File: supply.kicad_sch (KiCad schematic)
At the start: 186 parts, among them J7 BarrelJack_Pin2mm_MJ-179PH, J8 JST_SH_1x4_BM04B-SRSS-TB-LF-SN, Q12 SI7613DN-T1-GE3, Q13 SI7613DN-T1-GE3, Q14 BSS138PW, Q15 BSS138PW, Q16 BSS138PW, Q17 BSS138PW, SW4 SW_CVS-08TB, SW5 SW_KMR211NGLFS_SMD, U17 LTC4412IS6, U18 LTC4412IS6, U19 MPM54304GMN, U20 MPM54304GMN, U21 NCP718BSN330T1G, U22 MAX16150A_SOT, U25 PAC1954T-E_VQFN, U26 MAX812REUS+T, U28 XC6230H001ER-G, U29 MCP4726A0T_DFN, U30 PAC1954T-E_VQFN, U31 LM3880, U36 MP8796B, U37 MP8796B

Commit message: [#66300] Finish reconnecting power supply to support US+ voltages and power sequence
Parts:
- removed C205, C216, C220: C_100n_0402, antmicro-footprints:C_0402_1005Metric, symbol antmicroCapacitors0402:C_100n_0402
- removed C206: C_1u_0402, antmicro-footprints:C_0402_1005Metric, symbol antmicroCapacitors0402:C_1u_0402
- removed C207, C211, C218: C_10u_6.3V_0402, antmicro-footprints:C_0402_1005Metric, symbol antmicroCapacitors0402:C_10u_6.3V_0402
- removed R180: R_4k7_0402, antmicro-footprints:R_0402_1005Metric, symbol antmicroResistors0402:R_4k7_0402
- removed R182: R_10k_0402, antmicro-footprints:R_0402_1005Metric, symbol antmicroResistors0402:R_10k_0402
- removed R183: R_0R_22.4A_0603, antmicro-footprints:R_0603_1608Metric, symbol antmicroResistors0603:R_0R_22.4A_0603
- removed TP14: TP_1206_SMD_RCW-0C, antmicro-footprints:TP_1206_SMD_RCW-0C, symbol antmicroTestPoints:TP_1206_SMD_RCW-0C
- removed TP17: TP_1mm_SMD, antmicro-footprints:TP_SMD_1mm, symbol antmicroTestPoints:TP_1mm_SMD
- removed U28: XC6230H001ER-G, antmicro-footprints:Torex_USP-6C, symbol antmicroPMICVoltageRegulatorsLinear:XC6230H001ER-G
- removed U29: MCP4726A0T_DFN, antmicro-footprints:DFN-6-1EP_2x2mm_P0.65mm_EP1x1.6mm, symbol antmicroDataAcquisitionDigitaltoAnalogConvertersDAC:MCP4726A0T_DFN
- removed U30: PAC1954T-E_VQFN, antmicro-footprints:VQFN-16-1EP_3x3mm_P0.5mm_EP1.1x1.1mm, symbol antmicroPowerMeasurement:PAC1954T-E_VQFN
- added C201, C202: C_22u_25V_0805, antmicro-footprints:C_0805_2012Metric, symbol antmicroCapacitorsmisc:C_22u_25V_0805
- added TP14: TP_1mm_SMD, antmicro-footprints:TP_SMD_1mm, symbol antmicroTestPoints:TP_1mm_SMD
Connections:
- net sp_SEN_+ is gone; now on net MGTAVCC_SEN_+: NT3.1, U25.8 (IN3+)
- net sp_SEN_- is gone; now on net MGTAVCC_SEN_-: NT11.1, U25.7 (IN3-)
- net spare is gone; now on net +1V0_MGTAVCC: NT11.2, R143.2
- net +1V0_MGTAVCC: now also TP14.1; no longer NT9.2, R141.2, TP8.1
- net +1V2_MGTAVTT: now also NT10.2, R142.2, TP15.1
- net +1V8: now also NT9.2, R141.2, TP8.1; no longer NT10.2, R142.2, TP15.1
- net 1V8_SEN_+: now also NT1.1, U25.11 (IN1+); no longer NT2.1, U25.13 (IN2+)
- net 1V8_SEN_-: now also NT9.1, U25.12 (IN1-); no longer NT10.1, U25.14 (IN2-)
- net 1V8_local: now also C182.2, C186.2, NT1.2, R141.1, R151.2, U19.14 (VOUT1), U19.15 (VOUT1); no longer C183.2, C187.2, NT2.2, R142.1, R153.2, U19.8 (VOUT2), U19.9 (VOUT2)
- net GND: now also C201.1, C202.1
- net MGTAVCC_SEN_+: no longer NT1.1, U25.11 (IN1+)
- net MGTAVCC_SEN_-: no longer NT9.1, U25.12 (IN1-)
- net MGTAVCC_local: now also C183.2, C187.2, NT2.2, R142.1, R153.2, U19.8 (VOUT2), U19.9 (VOUT2); no longer C182.2, C186.2, NT1.2, R141.1, R151.2, U19.14 (VOUT1), U19.15 (VOUT1)
- net VDC: now also U19.28 (VIN), U19.29 (VIN), C201.2, C202.2
- net 1V7 renamed +1V8_MGTVCCAUX
- net 1V7_SEN_+ renamed MGTAVCCAUX_SEN_+
- net 1V7_SEN_- renamed MGTAVCCAUX_SEN_-
- net 1V7_local renamed MGTAVCCAUX_local
- net spare_local renamed MGTAVTT_local
- new net MGTAVTT_SEN_+: NT2.1, U25.13 (IN2+)
- new net MGTAVTT_SEN_-: NT10.1, U25.14 (IN2-)
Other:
- note added: "MGTAVCCAUX"
- note removed: "1V2 Low noise"
- note removed: "I2C: 0x10"
- note removed: "I2C: 0x60"
- note removed: "MGTAVTT Low noise LDO"
- note removed: "Set to ~1V7"
- note removed: "VREF DAC"
- moved on the sheet: C171, C260, R170, TP18

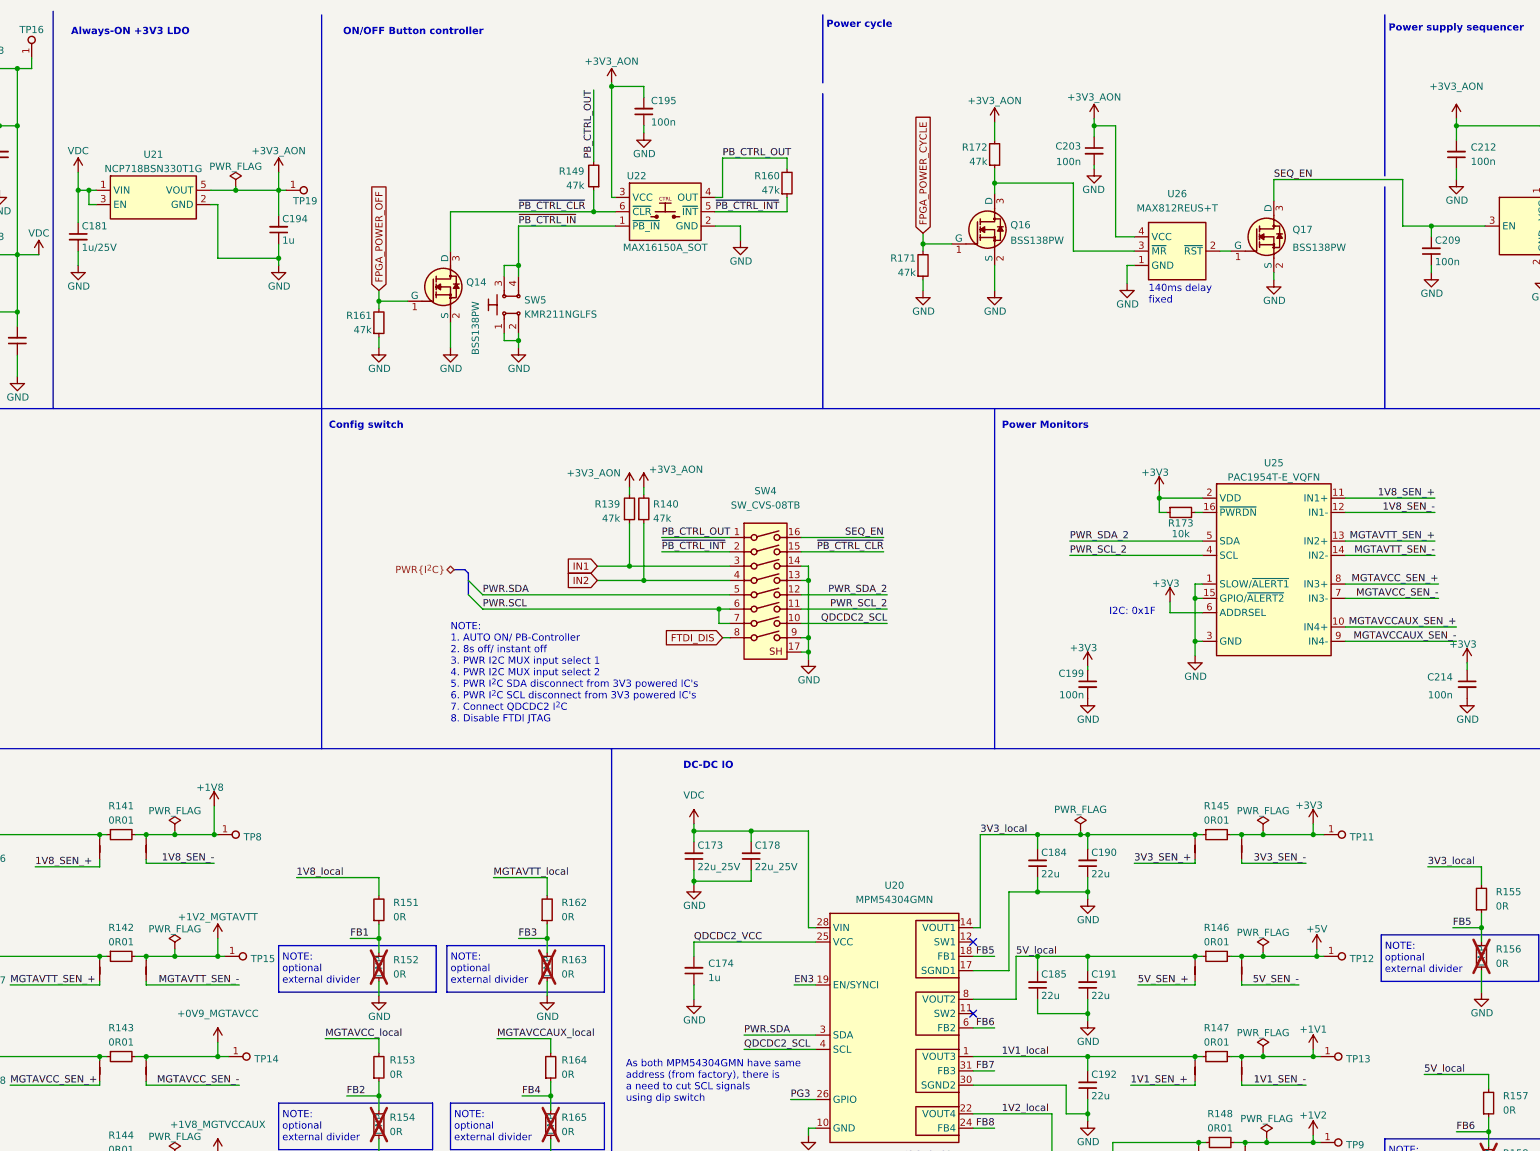
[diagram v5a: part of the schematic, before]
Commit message: [#66300] Replace MGTACC and MGTAVTT high side current measurement resistor, optimize decoupling
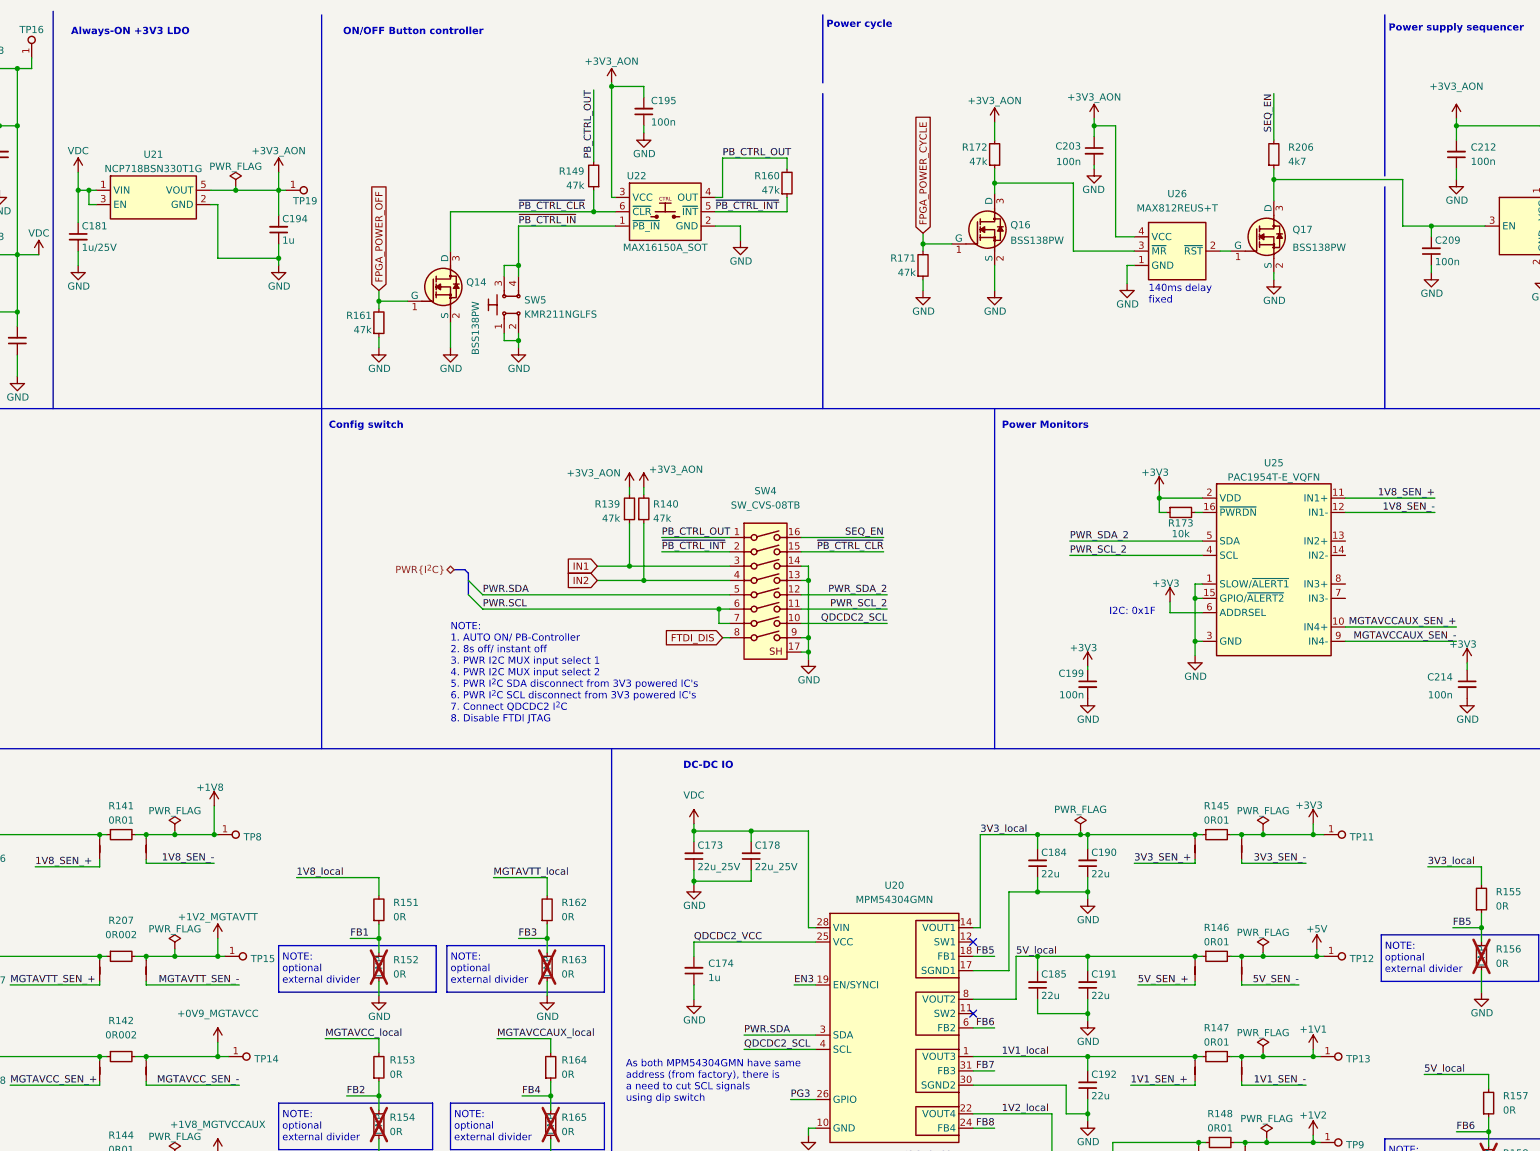
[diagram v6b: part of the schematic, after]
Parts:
- removed R142, R143: R_0R01_1206, antmicro-footprints:R_1206_3216Metric, symbol antmicroResistorsmisc:R_0R01_1206
- added R142, R207: R_0R002_0805, antmicro-footprints:R_0805_2012Metric, symbol antmicroResistorsmisc:R_0R002_0805
- added R206: R_4k7_0402, antmicro-footprints:R_0402_1005Metric, symbol antmicroResistors0402:R_4k7_0402
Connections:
- net +1V0_MGTAVCC: now also R142.2
- net +1V2_MGTAVTT: now also R207.2
- net MGTAVCC_SEN_+: no longer U25.8 (IN3+)
- net MGTAVCC_SEN_-: no longer U25.7 (IN3-)
- net MGTAVCC_local: now also R207.1
- net MGTAVTT_SEN_+: no longer U25.13 (IN2+)
- net MGTAVTT_SEN_-: no longer U25.14 (IN2-)
- net MGTAVTT_local: now also R142.1
- net SEQ_EN: now also R206.2; no longer C209.2, Q17.3 (D), U31.3 (EN)
- new net: C209.2, Q17.3 (D), R206.1, U31.3 (EN)

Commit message: [#66300] Replace power measurement IC's with PAC1720 and PAC1944. Split supply sheet to hierarchical structure. Add missing VCCINT pull-up resistors. Change power meters supply to 3V3_AON
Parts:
- removed C171, C173, C178, C201, C202, C260, C267, C268: C_22u_25V_0805, antmicro-footprints:C_0805_2012Metric, symbol antmicroCapacitorsmisc:C_22u_25V_0805
- removed C172, C174: C_1u_0402, antmicro-footprints:C_0402_1005Metric, symbol antmicroCapacitors0402:C_1u_0402
- removed C177, C266, C269, C272: C_4u7_25V_0402, antmicro-footprints:C_0402_1005Metric, symbol antmicroCapacitors0402:C_4u7_25V_0402
- removed C182, C183, C184, C185, C186, C187, C188, C189, C190, C191, C192, C193, C213, C215, C217, C219, C262, C263, C264, C265, C273, C274, C275, C276, C277, C278, C279, C280: C_22u_0603, antmicro-footprints:C_0603_1608Metric, symbol antmicroCapacitors0603:C_22u_0603
- removed C199, C214: C_100n_0402, antmicro-footprints:C_0402_1005Metric, symbol antmicroCapacitors0402:C_100n_0402
- removed C200: C_22n_0402, antmicro-footprints:C_0402_1005Metric, symbol antmicroCapacitors0402:C_22n_0402
- removed C259, C271: C_220n_16V_0402, antmicro-footprints:C_0402_1005Metric, symbol antmicroCapacitors0402:C_220n_16V_0402
- removed C261, C270: C_1u_25V_0402, antmicro-footprints:C_0402_1005Metric, symbol antmicroCapacitors0402:C_1u_25V_0402
- removed L2, L3: L_150n_30A_WE-HCM-7050, antmicro-footprints:L_WE-HCM-7050, symbol antmicroFixedInductors:L_150n_30A_WE-HCM-7050
- removed NT1, NT10, NT11, NT12, NT13, NT14, NT15, NT16, NT2, NT3, NT4, NT5, NT6, NT7, NT8, NT9: Net-Tie_P0.127mm, antmicro-footprints:NetTie-2_SMD_Pad0.127mm, symbol antmicroShuntsJumpers:Net-Tie_P0.127mm
- removed R141, R144, R145, R146, R147, R148: R_0R01_1206, antmicro-footprints:R_1206_3216Metric, symbol antmicroResistorsmisc:R_0R01_1206
- removed R142, R207: R_0R002_0805, antmicro-footprints:R_0805_2012Metric, symbol antmicroResistorsmisc:R_0R002_0805
- removed R151, R152, R153, R154, R155, R156, R157, R158, R162, R163, R164, R165, R166, R167, R168, R169, R181, R185, R186, R203: R_0R_0402, antmicro-footprints:R_0402_1005Metric, symbol antmicroResistors0402:R_0R_0402
- removed R173: R_10k_0402, antmicro-footprints:R_0402_1005Metric, symbol antmicroResistors0402:R_10k_0402
- removed R188, R189, R199, R200: R_0R_22.4A_0603, antmicro-footprints:R_0603_1608Metric, symbol antmicroResistors0603:R_0R_22.4A_0603
- removed R195: R_4k99_0402, antmicro-footprints:R_0402_1005Metric, symbol antmicroResistors0402:R_4k99_0402
- removed R196, R197: R_60k4_0402, antmicro-footprints:R_0402_1005Metric, symbol antmicroResistors0402:R_60k4_0402
- removed R198: R_3k4_0402, antmicro-footprints:R_0402_1005Metric, symbol antmicroResistors0402:R_3k4_0402
- removed R201: R_15k_0402, antmicro-footprints:R_0402_1005Metric, symbol antmicroResistors0402:R_15k_0402
- removed R202: R_8k16_0402, antmicro-footprints:R_0402_1005Metric, symbol antmicroResistors0402:R_8k16_0402
- removed R204, R205: R_10R_0402, antmicro-footprints:R_0402_1005Metric, symbol antmicroResistors0402:R_10R_0402
- removed TP10, TP11, TP12, TP13, TP14, TP15, TP18, TP23, TP8, TP9: TP_1mm_SMD, antmicro-footprints:TP_SMD_1mm, symbol antmicroTestPoints:TP_1mm_SMD
- removed U19, U20: MPM54304GMN, antmicro-footprints:LGA-33_7x7mm_P0.65mm, symbol antmicroPMICVoltageRegulatorsDCDCSwitchingRegulators:MPM54304GMN
- removed U25: PAC1954T-E_VQFN, antmicro-footprints:VQFN-16-1EP_3x3mm_P0.5mm_EP1.1x1.1mm, symbol antmicroPowerMeasurement:PAC1954T-E_VQFN
- removed U36, U37: MP8796B, symbol antmicroDCDCConverters:MP8796B
- added C207: C_100n_0402, antmicro-footprints:C_0402_1005Metric, symbol antmicroCapacitors0402:C_100n_0402
- added U29: AT24CS01_SOT23, antmicro-footprints:SOT-23-5, symbol antmicroMemory:AT24CS01_SOT23
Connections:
- net +3V3 is gone; now on net +3V3_AON: R135.2
- net +3V3_AON: now also C207.1, U29.4 (VCC)
- net GND: now also C207.2, U29.2 (GND), U29.5 (WP)
- net PWR.SCL: now also U29.1 (SCL); no longer SW4.6
- net PWR.SDA: now also U29.3 (SDA); no longer SW4.5
- net PWR_SCL_2: no longer names the net of SW4.11
- net PWR_SDA_2: no longer names the net of SW4.12
- no-connect marks 8 -> 7
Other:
- added sheet DC-DC AUX, MGT (dc-dc-aux-mgt.kicad_sch)
- added sheet DC-DC IO (dc-dc-io.kicad_sch)
- added sheet DC-DC VCCINT (dc-dc-vccint.kicad_sch)
- note added: "DC-DCs"
- note added: "NOTE: 1. AUTO ON/ PB-Controller 2. 8s off/ instant off 3. PWR I2C MUX input select 1 4. PWR I2C MUX input select 2 5. - 6. - 7. Connect QDCDC2 I^{2}C 8. Disable FTDI JTAG"
- note added: "UID"
- note removed: "+1V1"
- note removed: "+1V2"
- note removed: "+1V8"
- note removed: "+3V3"
- note removed: "+5V"
- note removed: "1 2 3 4"
- note removed: "As both MPM54304GMN have same address (from factory), there is a need to cut SCL signals using dip switch"
- note removed: "DC-DC AUX, MGT"
- note removed: "DC-DC INT"
- note removed: "DC-DC IO"
- note removed: "I2C: 0x1F"
- note removed: "I2C: 0x30"
- note removed: "I2C: 0x31"
- note removed: "I2C: 0x68"
- note removed: "I2C: 0x69"
- note removed: "MGTAVCC"
- note removed: "MGTAVCCAUX"
- note removed: "MGTAVTT"
- note removed: "NOTE: 1. AUTO ON/ PB-Controller 2. 8s off/ instant off 3. PWR I2C MUX input select 1 4. PWR I2C MUX input select 2 5. PWR I^{2}C SDA disconnect from 3V3 powered IC's 6. PWR I^{2}C SCL disconnect from 3V3 powered IC's 7. Connect QDCDC2 I^{2}C 8. Disable FTDI JTAG"
- note removed: "NOTE: optional external divider"
- note removed: "Pin compatible PN: MPQ8645P, MPQ8655GVT, MP8796K"
- note removed: "Power Monitors"
- note removed: "Second phase is for VCCINT > 20A applications"
- note removed: "Soft start delay time slot"
- note removed: "X"
- note removed: "remove after bringup"
- moved on the sheet: C198, J8, Q15, R135, R136, R137, R138, R139, R140, R170, SW4, TP20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

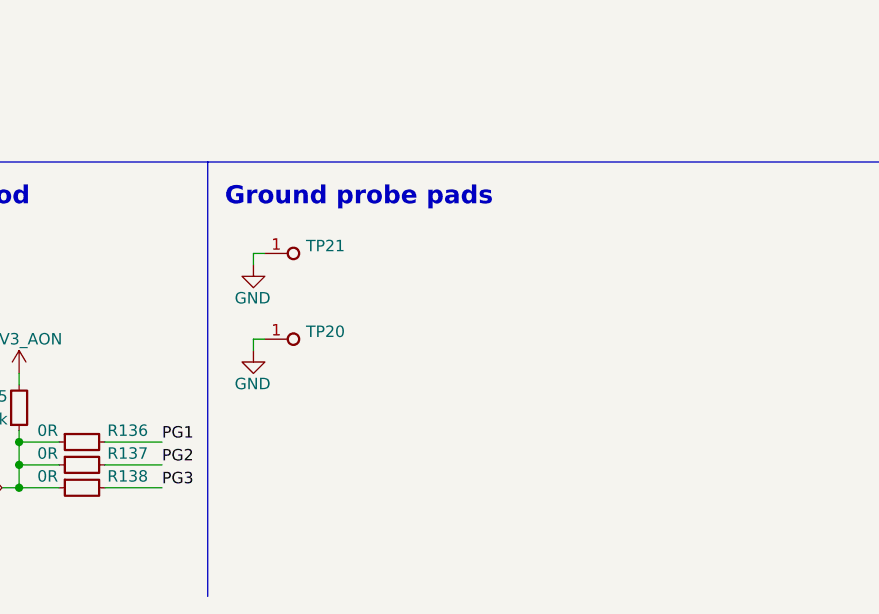
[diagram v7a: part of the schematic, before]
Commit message: [#66727] Continue routing low speed signals
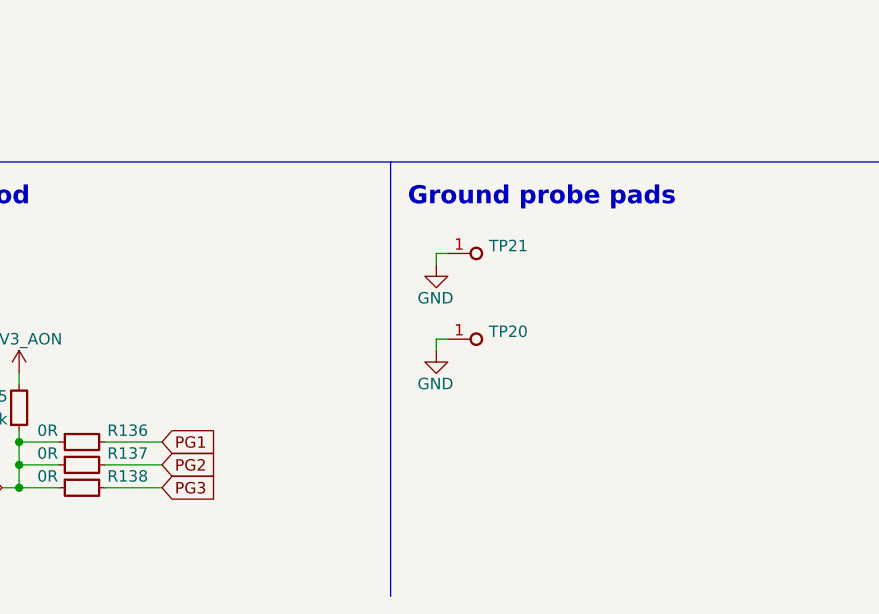
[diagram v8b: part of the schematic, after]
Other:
- moved on the sheet: TP20, TP21
